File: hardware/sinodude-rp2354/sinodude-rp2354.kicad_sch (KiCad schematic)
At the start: 96 parts, among them J1 USB-C, J2 SWD TC2030, J3 I2C, J4 DUT, Q1 2N7002, SW1 BOOTSEL, SW2 RESET, U1 RP2354A, U2 AMS1117-3.3, U3 TPS2114APW, U4 SN74LVC8T245PW, U5 SN74LVC1T45DBV, U6 SN74LVC1T45DBV, Y1 12MHz/CL10pF/ESR50R/ABM8-272-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

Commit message: hardware: tie U4 unused B-port pins to GND
The SN74LVC8T245 datasheet is explicit that both ports need this, not
just the input side. Section 8.1: "It is recommended to tie all unused
I/Os to GND. The device should not have any floating I/Os when changing
translation direction." The overview adds that "the input circuitry on
both A and B ports is always active and must have a logic HIGH or LOW
level applied to prevent excess ICC and ICCZ."

The input receiver stays powered on a pin even while that pin is driven
as an output, so a floating B5-B8 still presents a floating CMOS input
internally and still draws ICC. Every A and B pin is typed I/O in the pin
table, not "output", so the "tie all unused I/Os" wording covers them.

B5-B8 had no-connect flags; they are now GND. Safe because DIR is
hardwired to VCCA, so the direction never reverses and those pins sit
driving low into GND. Were DIR ever driven, both sides would need series
resistors rather than hard ties - noted on the sheet.

ERC is still 0 errors; the warning count goes 4 -> 8, same pin_to_pin
warning about a bidirectional pin on a net carrying a PWR_FLAG.

Also adds the page title block, which was empty.
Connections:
- net GND: now also U4.14 (B8), U4.15 (B7), U4.16 (B6), U4.17 (B5)
- no-connect marks 24 -> 20
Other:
- note added: "U4 A5-A8 and B5-B8 tied to GND: the input receiver stays active on both"
- note added: "ports, so a floating pin draws excess ICC. Safe only because DIR is"
- note added: "strapped to VCCA. If DIR ever becomes driven, these need series resistors."

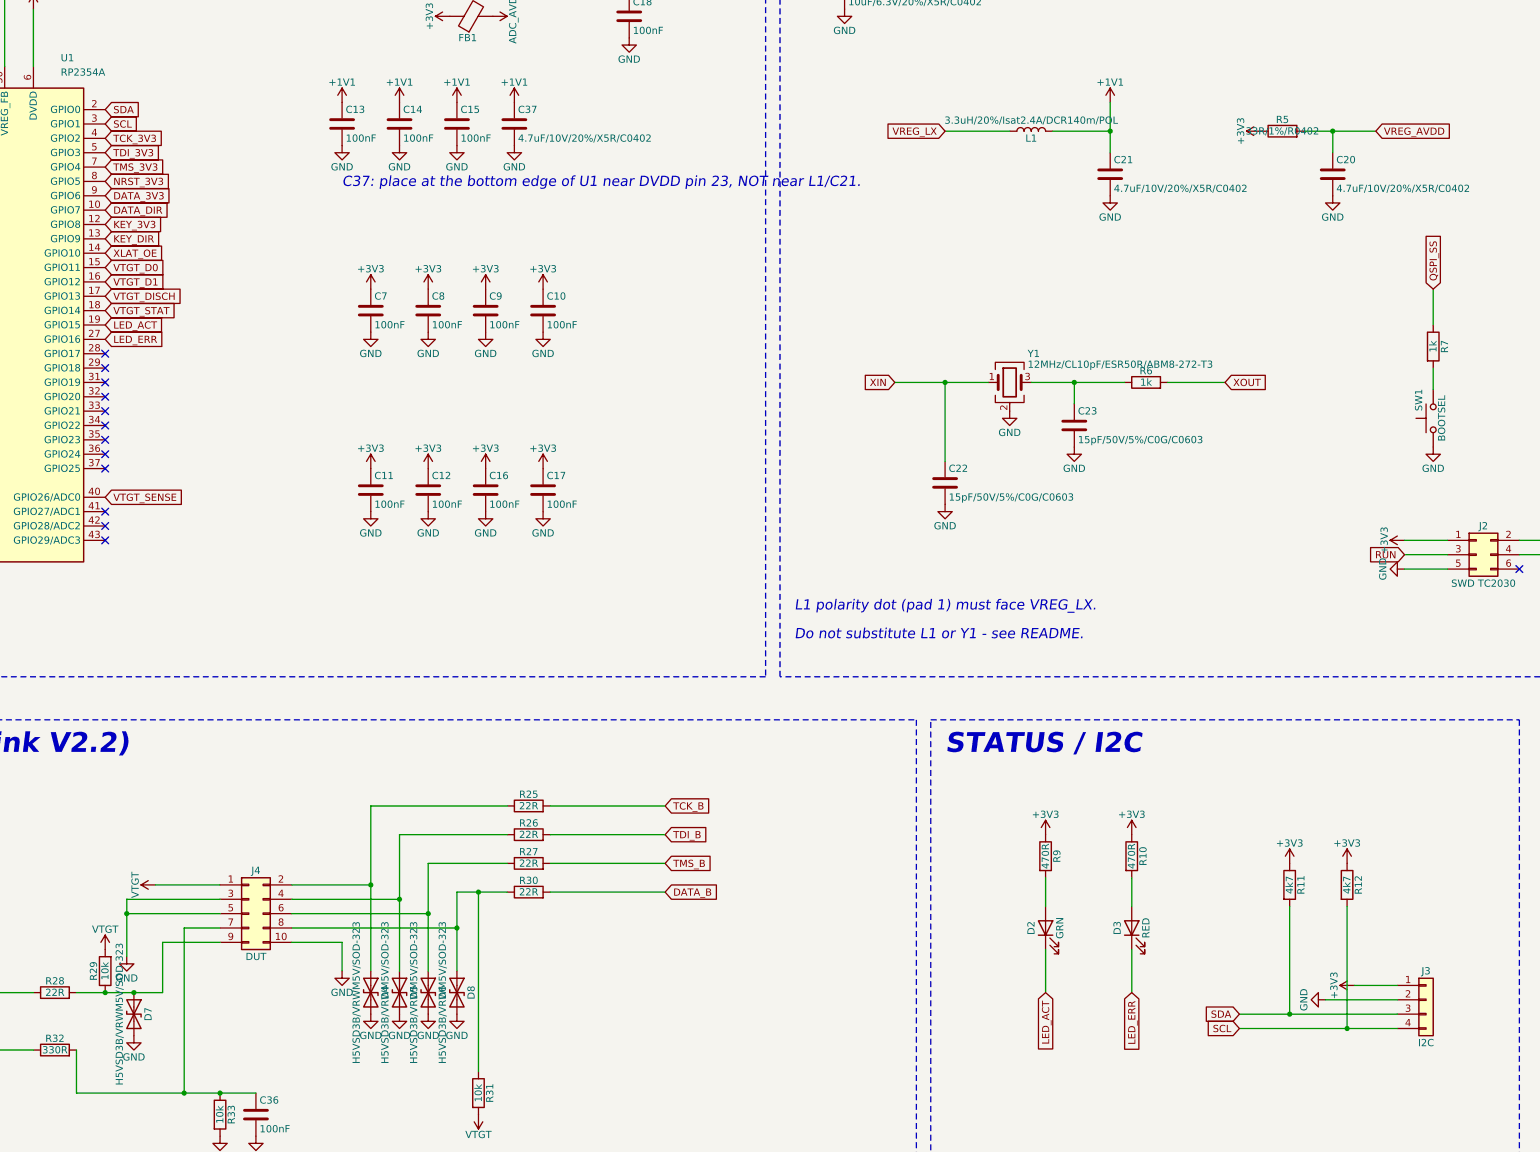
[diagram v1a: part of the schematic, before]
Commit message: hardware: remove the I2C header
J3 and its pull-ups R11/R12 were carried over from the board this design
started from, where the header drove a status display. Nothing in
sinodude uses I2C - the Rust tool and the AVR firmware have no reference
to it - so the header was speculative and is now gone.

GPIO0 and GPIO1 get no-connect flags. GPIO0 is XIP_CS1n, the chip select
for a second QSPI memory, so leaving it free is more useful than an
unused header.

93 components, ERC still 0 errors.

Also corrects two things in the README:

- TPS2114A was described as a 2004-era part needing a lifecycle check.
  TI lists both the TPS2114A and TPS2115A as ACTIVE. The problem is only
  that JLCPCB does not stock it, which is a distributor question.
- Drops the prior-art reference to the earlier board.
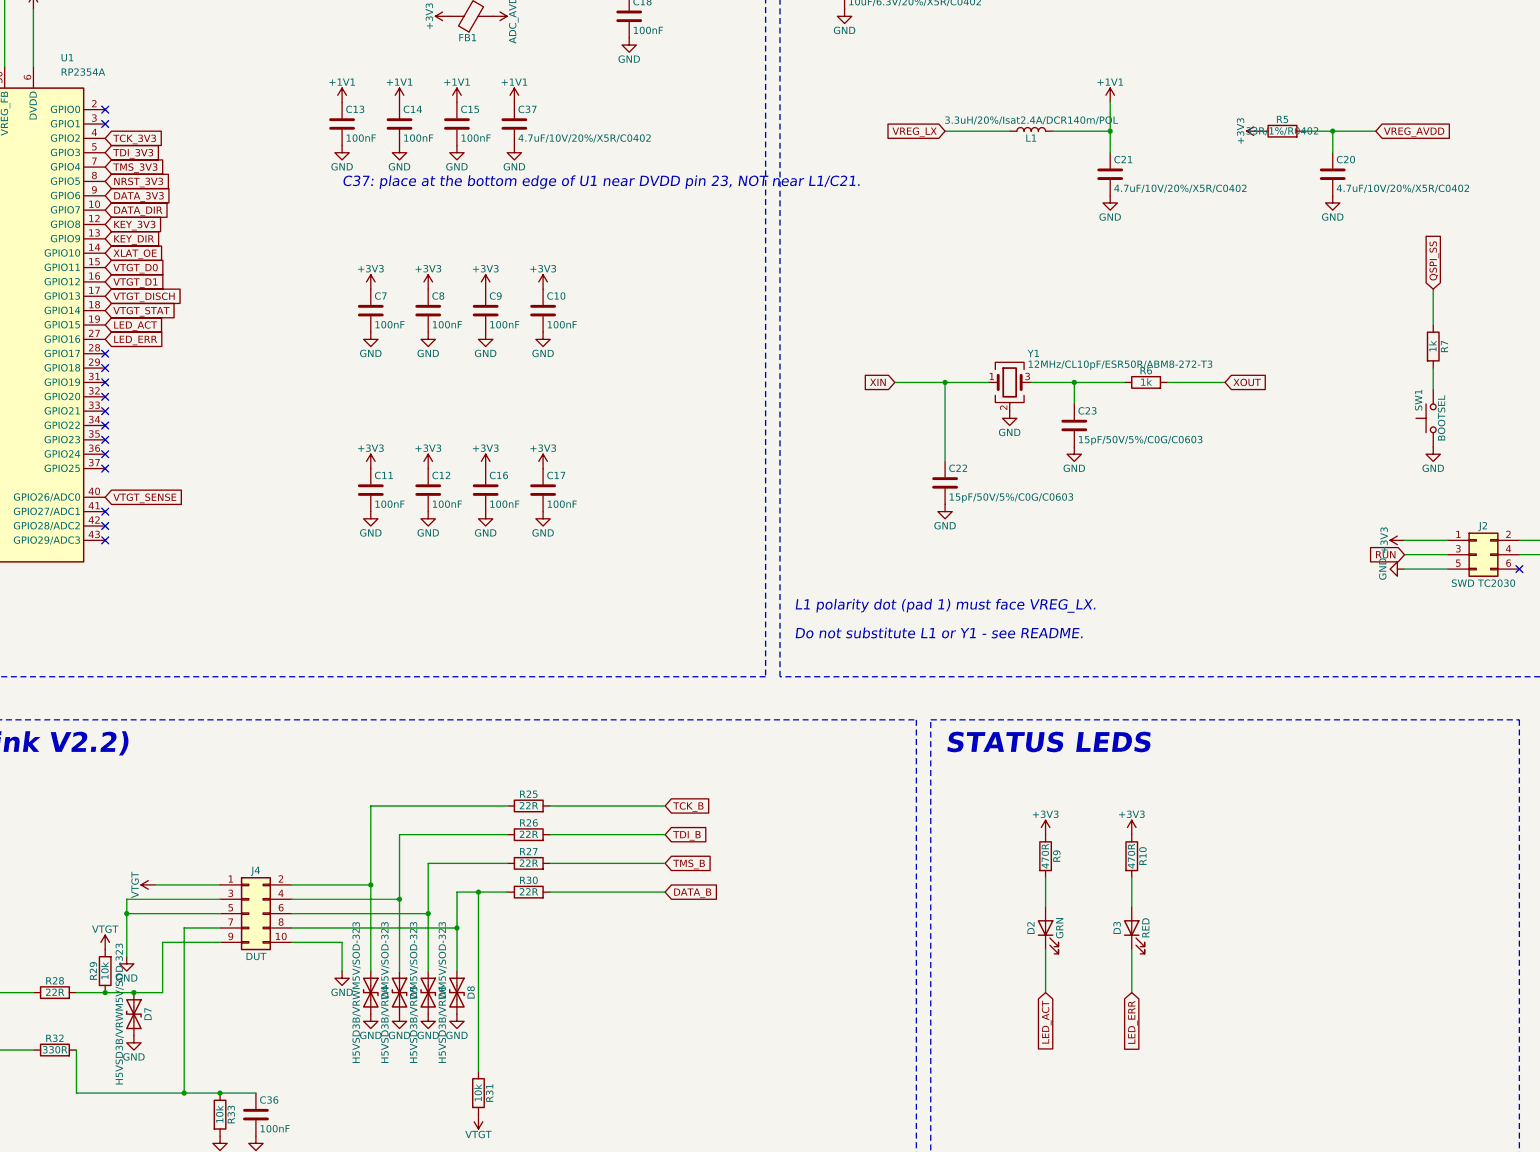
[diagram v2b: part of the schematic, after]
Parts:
- removed J3: I2C, Connector_PinHeader_2.54mm:PinHeader_1x04_P2.54mm_Vertical, symbol Connector_Generic:Conn_01x04
- removed R11, R12: 4k7, Resistor_SMD:R_0603_1608Metric, symbol Device:R
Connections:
- net SCL: no longer names the net of U1.3 (GPIO1)
- net SDA: no longer names the net of U1.2 (GPIO0)
- no-connect marks 20 -> 22
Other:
- note added: "STATUS LEDS"
- note removed: "STATUS / I2C"

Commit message: hardware: resolve U3, J1 and SW1/SW2 part numbers
My earlier searches of the JLCPCB catalogue were wrong in two ways: they
filtered on Stock>0, which hides the 71k zero-stock but orderable
entries, and they used ORDER BY with LIMIT, which truncated away exact
matches. Redoing them unfiltered turns up the right parts.

  U3       C118265   TPS2114APWR              0 stock, orderable, $1.92
  SW1/SW2  C72443    C&K KMR221GLFS           9727
  J1       C2894897  HCTL HC-TYPE-C-16P-01A   45815

SW1/SW2 and J1 are exact matches for the footprints already drawn - the
KiCad footprints are literally named after those parts.

LCSC coverage is now 89 of 93. What remains is H1-H4 (mounting holes),
J2 (Tag-Connect pads) and J4.

J4 is a real decision rather than a lookup: the footprint is a
right-angle shrouded box header, and the well-stocked LCSC 2x5 2.54mm
box header C5665 is vertical. No right-angle 2.54mm 2x5 shrouded box
header appears in the catalogue; the "Bent" parts are plain pin headers
and would lose the keying.

Also corrects the README claim that the TPS2114A is absent from the
catalogue, and records why the TPS2115A is not a valid substitute: the
ILIM constant is 500 rather than 250, putting 333mA below its
characterised range.
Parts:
- J1: LCSC (none) -> C2894897
- SW1, SW2: LCSC (none) -> C72443
- U3: LCSC (none) -> C118265
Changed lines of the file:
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@@
 			)
 		)
-	)
+		(property "LCSC" "C72443"
+			(at 340.36 256.54 0)
+			(hide yes)
+			(effects
+				(font
+					(size 1.27 1.27)
+				)
+			)
+		))
 	(symbol
 		(lib_id "power:+3V3")
@@
 			)
 		)
-	)
+		(property "LCSC" "C2894897"
+			(at 34.29 76.2 0)
+			(hide yes)
+			(effects
+				(font
+					(size 1.27 1.27)
+				)
+			)
+		))
 	(symbol
 		(lib_id "power:+3.3VA")
@@
 			)
 		)
-	)
+		(property "LCSC" "C72443"
+			(at 379.73 256.54 0)
+			(hide yes)
+			(effects
+				(font
+					(size 1.27 1.27)
+				)
+			)
+		))
 	(symbol
 		(lib_id "power:GND")
@@
 			)
 		)
-	)
+		(property "LCSC" "C118265"
+			(at 312.42 76.2 0)
+			(hide yes)
+			(effects
+				(font
+					(size 1.27 1.27)
+				)
+			)
+		))
 	(symbol
 		(lib_id "Device:C")

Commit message: hardware: J4 gets a right-angle IDC box header part
C5156674, ZHOURI DC3-2.54-10PAL - 2x5 2.54mm shrouded IDC box header,
right angle, 3172 in stock. Exact match for the
IDC-Header_2x05_P2.54mm_Horizontal footprint already drawn, so no
footprint change is needed.

The DC3 family encodes orientation in one letter of the suffix: -10PAS
is vertical, -10PAL is right angle. My earlier searches missed the PAL
because they looked for "box", "shrouded" or "Bent" in the part name,
and this one only gives it away in a Chinese-language description field.

Every component that is physically placed now carries an LCSC number:
88 of 93. The remaining 5 are H1-H4, which are drilled holes, and J2,
which is the bare Tag-Connect pad pattern - neither is a part.
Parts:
- J4: LCSC (none) -> C5156674
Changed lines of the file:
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@@
 			)
 		)
-	)
+		(property "LCSC" "C5156674"
+			(at 130.81 344.17 0)
+			(hide yes)
+			(effects
+				(font
+					(size 1.27 1.27)
+				)
+			)
+		))
 	(symbol
 		(lib_id "Device:R")

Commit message: hardware: 3D models for every physical part
Three separate gaps, all closed.

flake.nix never exported KICAD10_3DMODEL_DIR, so in the dev shell no 3D
model resolved at all - every footprint references that variable and it
was undefined. One line.

The KiCad 3D library ships no QFN-60 model. It has QFN-52 and QFN-56 in
7x7, but not 60, so the RP2354A had no body. Built one in FreeCAD to the
RP2350 datasheet Figure 143 nominals: D/E 7 BSC, A 0.85, A1 0.02, A3
0.203 REF, D2/E2 3.40, b 0.18, e 0.400 BSC, L 0.40. Verified bounding box
7.000 x 7.000 x 0.850, single valid solid, origin centred, seating plane
at z=0. Same for the custom Abracon inductor footprint, to 2.00 x 1.60 x
1.00 max.

These are visual and mechanical-fit models, not vendor CAD - nominal lead
geometry, no internal detail.

Since a model hangs off a footprint, QFN-60-...ThermalVias is copied into
footprints/sinodude.pretty with its model path retargeted. Otherwise
identical to stock, and it will not track upstream fixes.

J1 moves from the HCTL to the GCT USB4105 receptacle, C5184243
(USB4105-GF-A-120, 16P, 4143 in stock). The HCTL footprint referenced a
model the library does not ship; GCT has an identical pad set, so this is
a footprint swap with no schematic change. The -120 suffix matters: plain
-GF-A and -060 are 12-pin parts.

Amphenol was the obvious alternative but its footprint is a 24-pad USB 3.x
receptacle, which would not fit the USB 2.0 16P symbol.

ERC still 0 errors.
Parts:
- J1: footprint Connector_USB:USB_C_Receptacle_HCTL_HC-TYPE-C-16P-01A -> Connector_USB:USB_C_Receptacle_GCT_USB4105-xx-A_16P_TopMnt_Horizontal; LCSC C2894897 -> C5184243
- U1: footprint Package_DFN_QFN:QFN-60-1EP_7x7mm_P0.4mm_EP3.4x3.4mm_ThermalVias -> sinodude:QFN-60-1EP_7x7mm_P0.4mm_EP3.4x3.4mm_ThermalVias
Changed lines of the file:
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@@
 			)
 		)
-		(property "Footprint" "Package_DFN_QFN:QFN-60-1EP_7x7mm_P0.4mm_EP3.4x3.4mm_ThermalVias"
+		(property "Footprint" "sinodude:QFN-60-1EP_7x7mm_P0.4mm_EP3.4x3.4mm_ThermalVias"
 			(at 80.01 240.03 0)
 			(hide yes)
@@
 			)
 		)
-		(property "Footprint" "Connector_USB:USB_C_Receptacle_HCTL_HC-TYPE-C-16P-01A"
+		(property "Footprint" "Connector_USB:USB_C_Receptacle_GCT_USB4105-xx-A_16P_TopMnt_Horizontal"
 			(at 34.29 76.2 0)
 			(hide yes)
@@
 			)
 		)
-		(property "LCSC" "C2894897"
+		(property "LCSC" "C5184243"
 			(at 34.29 76.2 0)
 			(hide yes)
